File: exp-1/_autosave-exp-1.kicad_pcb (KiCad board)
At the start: 2 copper layers, 14 parts

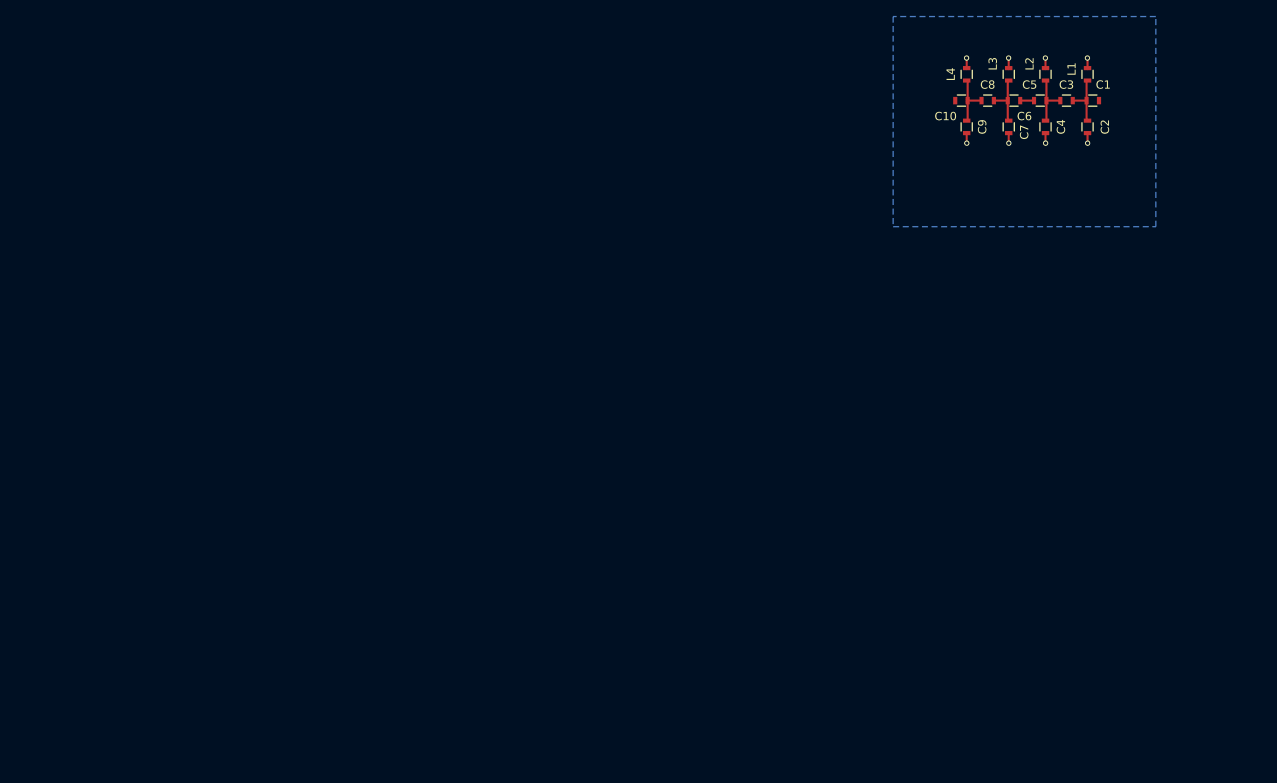
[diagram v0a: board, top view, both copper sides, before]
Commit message: More work done on copying DSP-10. Layout started.
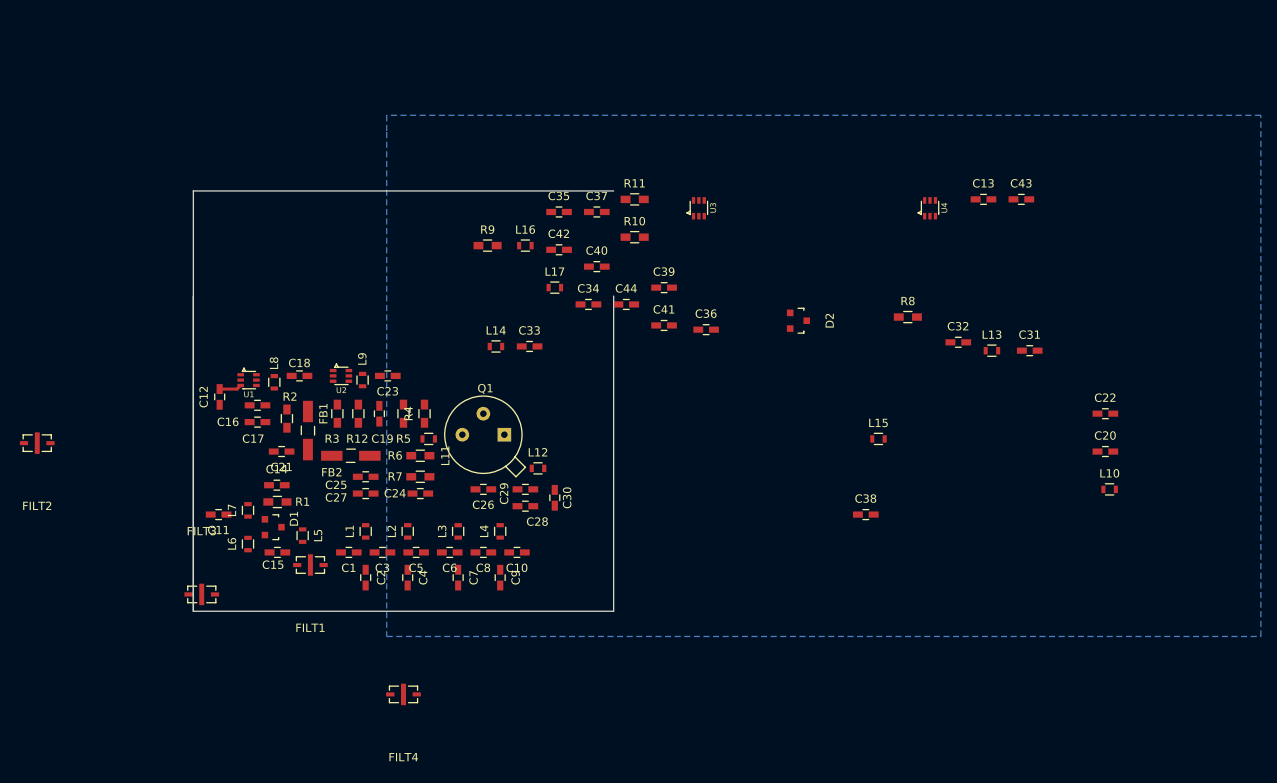
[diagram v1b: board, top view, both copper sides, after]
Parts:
- added C11: 15p, Capacitors_SMD:C_0603_HandSoldering, F.Cu at (77.2, 142.7)
- added C12: 470p, Capacitors_SMD:C_0603_HandSoldering, F.Cu at (77.3, 128.5)
- added C13: 470p, Capacitors_SMD:C_0603_HandSoldering, F.Cu at (169.7, 104.6)
- added C14: .01u, Capacitors_SMD:C_0603_HandSoldering, F.Cu at (84.3, 139.2)
- added C15: .01u, Capacitors_SMD:C_0603_HandSoldering, F.Cu at (84.3, 147.3)
- added C16: .01u, Capacitors_SMD:C_0603_HandSoldering, F.Cu at (81.9, 129.5)
- added C17: .01u, Capacitors_SMD:C_0603_HandSoldering, F.Cu at (81.9, 131.6)
- added C18: 470p, Capacitors_SMD:C_0603_HandSoldering, F.Cu at (87.0, 126.0)
- added C19: .01u, Capacitors_SMD:C_0603_HandSoldering, F.Cu at (96.7, 130.6)
- added C20: 470p, Capacitors_SMD:C_0603_HandSoldering, F.Cu at (184.4, 135.1)
- added C21: .01u, Capacitors_SMD:C_0603_HandSoldering, F.Cu at (84.8, 135.1)
- added C22: .01u, Capacitors_SMD:C_0603_HandSoldering, F.Cu at (184.4, 130.6)
- added C23: 470p, Capacitors_SMD:C_0603_HandSoldering, F.Cu at (97.7, 126.0)
- added C24: .01u, Capacitors_SMD:C_0603_HandSoldering, F.Cu at (101.6, 140.2)
- added C25: .01u, Capacitors_SMD:C_0603_HandSoldering, F.Cu at (95.0, 138.2)
- added C26: 15p, Capacitors_SMD:C_0603_HandSoldering, F.Cu at (109.2, 139.7)
- added C27: .01u, Capacitors_SMD:C_0603_HandSoldering, F.Cu at (95.0, 140.2)
- added C28: 15p, Capacitors_SMD:C_0603_HandSoldering, F.Cu at (114.3, 141.7)
- added C29: 8.2p, Capacitors_SMD:C_0603_HandSoldering, F.Cu at (114.3, 139.7)
- added C30: 15p, Capacitors_SMD:C_0603_HandSoldering, F.Cu at (117.9, 140.7)
- added C31: 470p, Capacitors_SMD:C_0603_HandSoldering, F.Cu at (175.3, 122.9)
- added C32: .01u, Capacitors_SMD:C_0603_HandSoldering, F.Cu at (166.6, 121.9)
- added C33: 47p, Capacitors_SMD:C_0603_HandSoldering, F.Cu at (114.8, 122.4)
- added C34: 12p, Capacitors_SMD:C_0603_HandSoldering, F.Cu at (121.9, 117.3)
- added C35: 1p, Capacitors_SMD:C_0603_HandSoldering, F.Cu at (118.4, 106.2)
- added C36: .01u, Capacitors_SMD:C_0603_HandSoldering, F.Cu at (136.1, 120.4)
- added C37: 12p, Capacitors_SMD:C_0603_HandSoldering, F.Cu at (122.9, 106.2)
- added C38: 470p, Capacitors_SMD:C_0603_HandSoldering, F.Cu at (155.4, 142.7)
- added C39: .01u, Capacitors_SMD:C_0603_HandSoldering, F.Cu at (131.1, 115.3)
- added C40: 47p, Capacitors_SMD:C_0603_HandSoldering, F.Cu at (122.9, 112.8)
- added C41: .01u, Capacitors_SMD:C_0603_HandSoldering, F.Cu at (131.1, 119.9)
- added C42: 33p, Capacitors_SMD:C_0603_HandSoldering, F.Cu at (118.4, 110.7)
- added C43: 470p, Capacitors_SMD:C_0603_HandSoldering, F.Cu at (174.2, 104.6)
- added C44: .01u, Capacitors_SMD:C_0603_HandSoldering, F.Cu at (126.5, 117.3)
- added D1: BAR15-1, Housings_SOT-23_SOT-143_TSOT-6:SOT-23, F.Cu at (83.8, 144.3)
- added D2: BAR15-1, Housings_SOT-23_SOT-143_TSOT-6:SOT-23, F.Cu at (147.3, 119.3)
- added FB1: FILTER, Choke_SMD:Choke_SMD_1206_Handsoldering, F.Cu at (88.0, 132.6)
- added FB2: FILTER, Choke_SMD:Choke_SMD_1206_Handsoldering, F.Cu at (93.2, 135.6)
- added FILT1: MTFILT, exp-1:FILTACH32T, F.Cu at (88.3, 148.8)
- added FILT2: MTFILT, exp-1:FILTACH32T, F.Cu at (55.3, 134.1)
- added FILT3: MTFILT, exp-1:FILTACH32T, F.Cu at (75.2, 152.4)
- added FILT4: MTFILT, exp-1:FILTACH32T, F.Cu at (99.6, 164.5)
- added L10: .33u, Resistors_SMD:R_0603, F.Cu at (184.9, 139.7)
- added L11: 100n, Resistors_SMD:R_0603, F.Cu at (102.6, 133.6)
- added L12: 39n, Resistors_SMD:R_0603, F.Cu at (115.8, 137.2)
- added L13: .33u, Resistors_SMD:R_0603, F.Cu at (170.7, 122.9)
- added L14: .33u, Resistors_SMD:R_0603, F.Cu at (110.7, 122.4)
- added L15: .33u, Resistors_SMD:R_0603, F.Cu at (157.0, 133.6)
- added L16: .33u, Resistors_SMD:R_0603, F.Cu at (114.3, 110.2)
- added L17: .33u, Resistors_SMD:R_0603, F.Cu at (117.9, 115.3)
- added L5: .33u, Resistors_SMD:R_0603, F.Cu at (87.4, 145.3)
- added L6: .33u, Resistors_SMD:R_0603, F.Cu at (80.8, 146.3)
- added L7: .33u, Resistors_SMD:R_0603, F.Cu at (80.8, 142.2)
- added L8: .33u, Resistors_SMD:R_0603, F.Cu at (84.0, 126.8)
- added L9: .33u, Resistors_SMD:R_0603, F.Cu at (94.6, 126.5)
- added Q1: 2n5109, Discret:TO39EBC, F.Cu at (109.2, 133.1)
- added R1: 680R, Resistors_SMD:R_0603_HandSoldering, F.Cu at (84.3, 141.2)
- added R10: 331R, Resistors_SMD:R_0603_HandSoldering, F.Cu at (127.5, 109.2)
- added R11: 331R, Resistors_SMD:R_0603_HandSoldering, F.Cu at (127.5, 104.6)
- added R12: 331R, Resistors_SMD:R_0603_HandSoldering, F.Cu at (94.1, 130.6)
- added R2: 121R, Resistors_SMD:R_0603_HandSoldering, F.Cu at (85.5, 131.1)
- added R3: 331R, Resistors_SMD:R_0603_HandSoldering, F.Cu at (91.6, 130.6)
- added R4: 3.3k, Resistors_SMD:R_0603_HandSoldering, F.Cu at (102.1, 130.6)
- added R5: 1K, Resistors_SMD:R_0603_HandSoldering, F.Cu at (99.6, 130.6)
- added R6: 2.2R, Resistors_SMD:R_0603_HandSoldering, F.Cu at (101.6, 135.6)
- added R7: 22R, Resistors_SMD:R_0603_HandSoldering, F.Cu at (101.6, 138.2)
- added R8: 680R, Resistors_SMD:R_0603_HandSoldering, F.Cu at (160.5, 118.9)
- added R9: 121R, Resistors_SMD:R_0603_HandSoldering, F.Cu at (109.7, 110.2)
- added U1: ABA-52563, exp-1:SOT_363, F.Cu at (79.9, 125.8)
- added U2: AVT-50663, exp-1:SOT_363, F.Cu at (91.1, 125.3)
- added U3: ABA-52563, exp-1:SOT_363, F.Cu at (134.6, 106.7)
- added U4: AVT-50663, exp-1:SOT_363, F.Cu at (162.6, 106.7)
- C1, C10, C2, C3, C4, C5, C6, C7, C8, C9: footprint Resistors_SMD:R_0603 -> Capacitors_SMD:C_0603_HandSoldering
- moved C1 105.2 mm to (93.0, 147.3), turned to 180 degrees
- moved L1 103.3 mm to (95.0, 144.8)
- moved C2 102.9 mm to (95.0, 150.4)
- moved C3 99.1 mm to (97.0, 147.3), turned to 180 degrees
- moved L2 94.8 mm to (100.1, 144.8)
- moved C4 94.4 mm to (100.1, 150.4)
- moved C5 93.1 mm to (101.1, 147.3), turned to 180 degrees
- moved C6 87.4 mm to (105.2, 147.3), turned to 180 degrees
- moved L3 86.5 mm to (106.2, 144.8)
- moved C7 86.0 mm to (106.2, 150.4)
- moved C8 81.8 mm to (109.2, 147.3), turned to 180 degrees
- moved L4 78.9 mm to (111.3, 144.8)
- moved C9 78.4 mm to (111.3, 150.4)
- moved C10 76.6 mm to (113.3, 147.3), turned to 180 degrees
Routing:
- net GND: track 10.7 -> 0.00 mm, vias 8 -> 0
- net Net-(C10-Pad2): track 6.95 -> 0.00 mm
- net Net-(C3-Pad1): track 6.62 -> 0.00 mm
- net Net-(C6-Pad1): track 6.62 -> 0.00 mm
- net Net-(C1-Pad1): track 6.62 -> 0.00 mm
- net Net-(C12-Pad2): track 0.00 -> 2.72 mm
- net Net-(C5-Pad1): track 1.68 -> 0.00 mm
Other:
- board outline added: 50.8 x 50.8 mm
- net class Default: trace_width 0.254 -> 0.3556
- rule trace_min: 0.1524 -> 0.1778

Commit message: Continued work on radio project thing
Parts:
- added L18, L19: 100n, Resistors_SMD:R_0603, F.Cu at (99.6, 164.5)
- added SL1: SDRSEL, exp-1:BSEL2, F.Cu at (99.6, 164.5)
- added U5: ADE-1, exp-1:PL-052, F.Cu at (117.3, 146.8)
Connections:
- C31 pad 1: Net-(C31-Pad1) -> /TX_SL
- D2 pad 1: Net-(C31-Pad1) -> Net-(C31-Pad2)
- L13 pad 1: Net-(C31-Pad1) -> Net-(C31-Pad2)
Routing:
- removed copper zone on B.Cu, net GND
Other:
- copper layers 2 -> 4
